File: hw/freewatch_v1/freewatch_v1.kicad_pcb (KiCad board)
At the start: 4 copper layers, 40 x 40 mm, 111 parts, among them P1 USB-MICRO-AB, P3 CONN_2, P6 CONN_2, P7 CONN_6, Q1 BSS138, Q2 BSS138, SW1 SW_PUSH, SW2 SW_PUSH, SW3 SW_PUSH, SW4 SW_PUSH, U1 PRTR5V0U2X, U10 MAX44009, U11 LSM303C, U12 MS5806-02BA, U13 ADP198, U14 LS013B7DH03, U15 EFM32GG330, U2 bq24072, U3 TPS780180300, U4 MAX17047, U5 TPS780180300, U6 M10478-A1, U7 MICRO_SDCARD_SPI, U8 ADP198, X1 32.768kHz, X2 48MHz

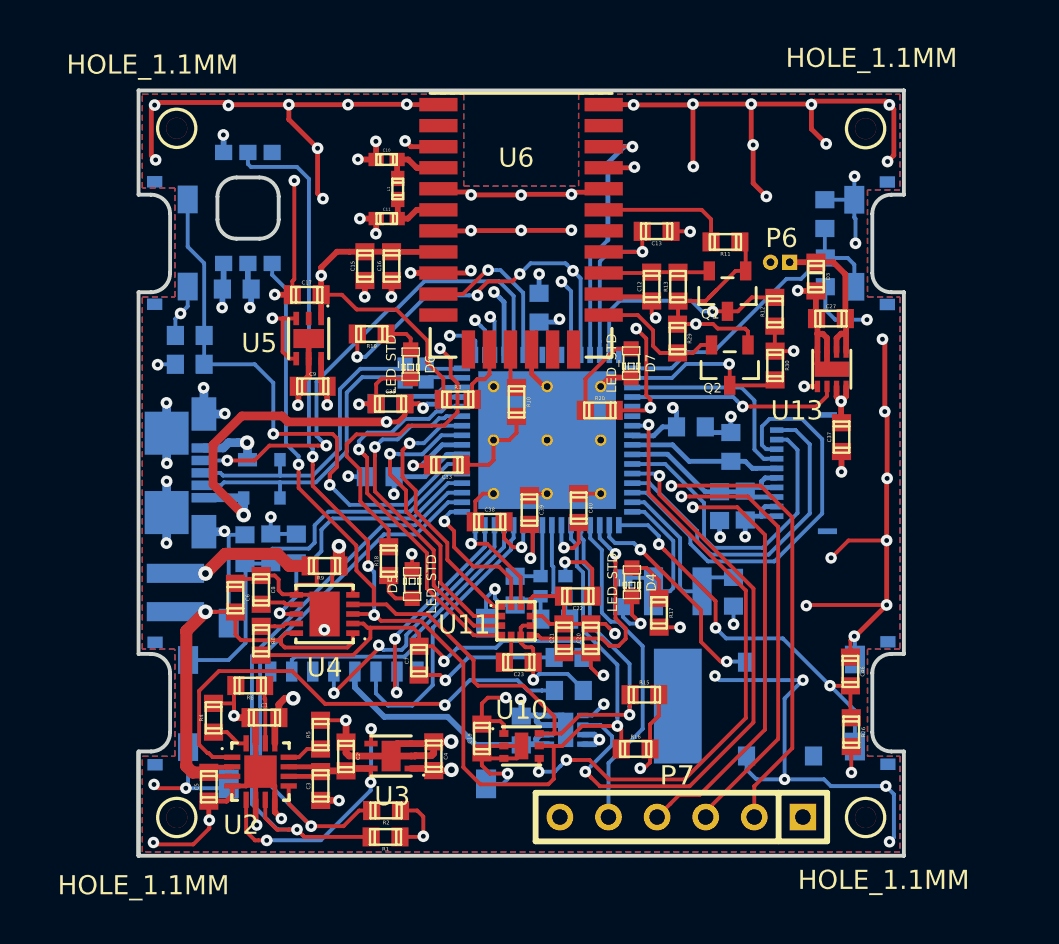
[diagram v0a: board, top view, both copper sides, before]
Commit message: hw: Add SPI flash memory for GPS module. Add SST25WF040B symbol and footprint.
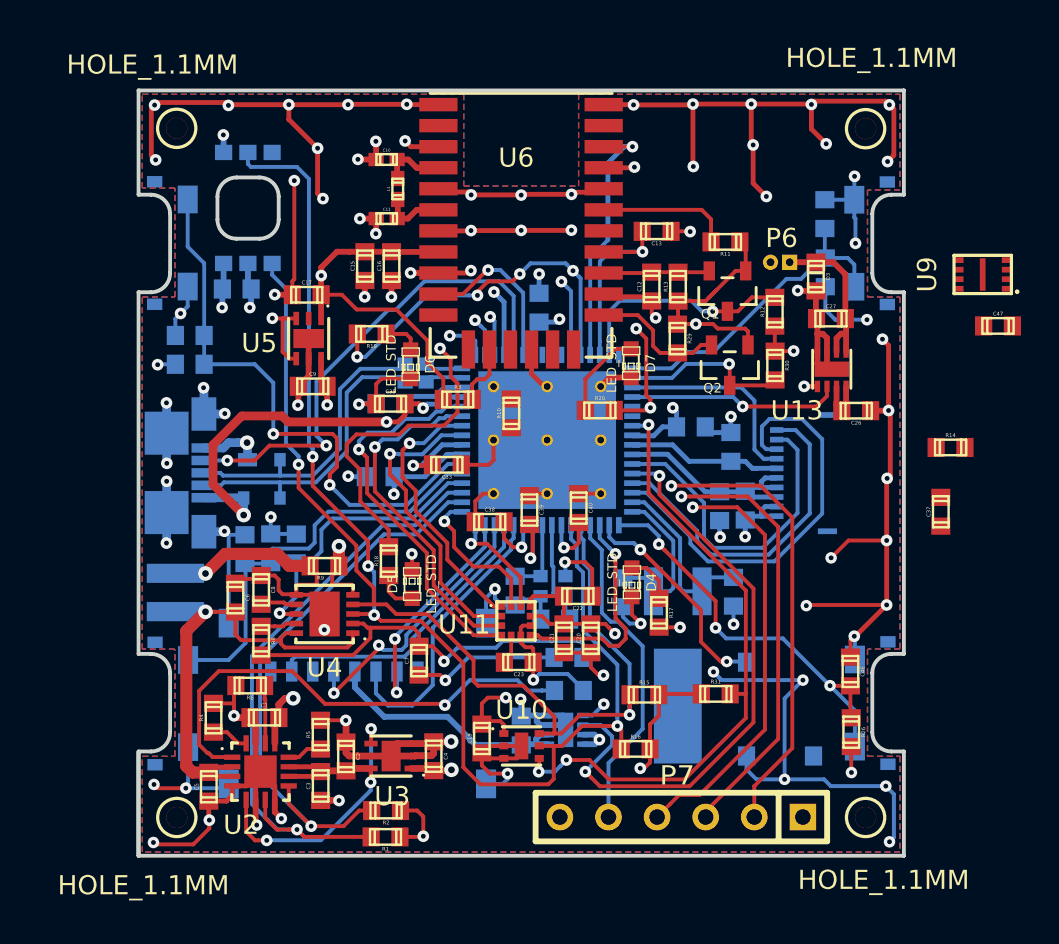
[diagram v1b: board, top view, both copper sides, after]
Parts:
- added C26: 10uF, Capacitors_SMD:c_0603, F.Cu at (123.8, 91.0)
- added C47: 100nF, Capacitors_SMD:c_0603, F.Cu at (131.2, 86.6)
- added R14: 10R, freewatch_footprints:r_0603, F.Cu at (128.7, 93.0)
- added R31: 100k, freewatch_footprints:r_0603, F.Cu at (116.5, 105.8)
- added U9: SST25WF040B, freewatch_footprints:USON_2X3, F.Cu at (130.4, 83.9)
- SW1, SW2, SW3, SW4: value SW_PUSH -> EVQ-P4MB3K
- moved C37 6.49 mm to (128.2, 96.3)
- moved R10 0.66 mm to (105.8, 91.2), turned to 90 degrees
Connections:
- C2 pad 1: Net-(C2-Pad1) -> +VIN
- C3 pad 1: Net-(C2-Pad1) -> +VIN
- C9 pad 1: VCC -> +VIN
- R10 pad 1: GND -> Net-(R10-Pad1)
- R10 pad 2: Net-(R10-Pad2) -> +1.8V
- U13 pad 7: VCC -> Net-(C26-Pad1)
- U13 pad 8: VCC -> Net-(C26-Pad1)
- U2 pad 10: Net-(C2-Pad1) -> +VIN
- U2 pad 11: Net-(C2-Pad1) -> +VIN
- U2 pad 5: Net-(C2-Pad1) -> +VIN
- U3 pad 4: Net-(C2-Pad1) -> +VIN
- U3 pad 6: Net-(C2-Pad1) -> +VIN
- U5 pad 4: VCC -> +VIN
- U5 pad 6: VCC -> +VIN
- U6 pad 14: Net-(R10-Pad2) -> Net-(R10-Pad1)
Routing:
- net +VIN: track 0.00 -> 23.5 mm, vias 0 -> 4
- net Net-(C2-Pad1): track 20.5 -> 0.00 mm, vias 3 -> 0
- net VCC: track 70.3 -> 66.8 mm, vias 23 -> 21
- net Net-(C26-Pad1): track 0.00 -> 2.74 mm
- net Net-(R10-Pad2): track 2.11 -> 0.00 mm
- net GND: track 294.7 -> 292.6 mm, vias 93 -> 92
- net LS_INT_N: track 31.9 -> 32.7 mm

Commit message: hw: Route SPI flash memory for GPS and 1.8V LDO + motor switch.
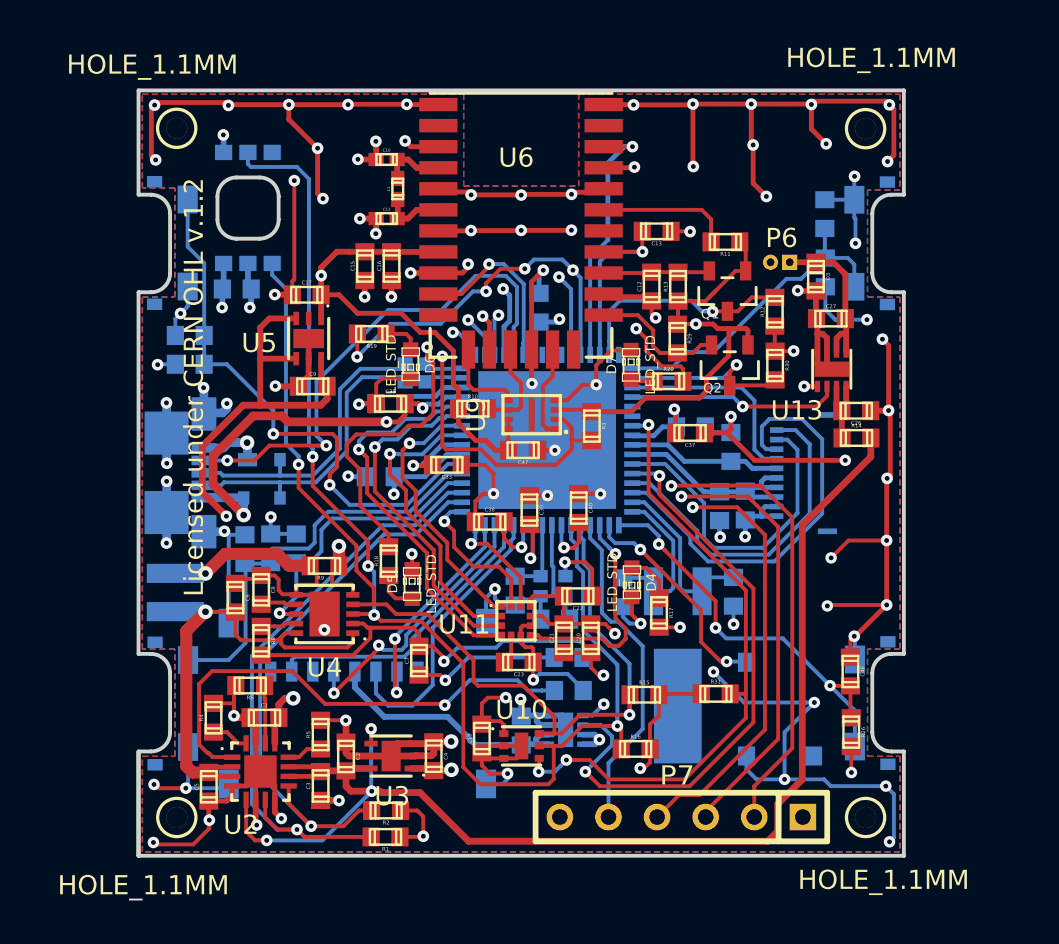
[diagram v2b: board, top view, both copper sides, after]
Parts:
- moved C47 25.7 mm to (106.4, 93.1), turned to 180 degrees
- moved U9 24.7 mm to (106.8, 91.2)
- moved C37 13.7 mm to (115.1, 92.2), turned to 180 degrees
- moved R3 7.15 mm to (110.0, 91.8), turned to 270 degrees
- moved R14 4.94 mm to (123.8, 92.5)
- moved R20 3.90 mm to (114.0, 89.5)
- moved R10 2.03 mm to (103.8, 90.9), turned to 0 degrees
- moved D7 0.09 mm to (112.0, 88.6), turned to 90 degrees
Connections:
- U5 pad 3: VCC -> +VIN
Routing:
- net +VIN: track 23.5 -> 108.9 mm
- net +1.8V: track 52.8 -> 72.1 mm
- net Net-(R3-Pad1): track 3.21 -> 21.6 mm, vias 0 -> 2
- net GND: track 292.6 -> 310.5 mm, vias 92 -> 99
- net Net-(R10-Pad1): track 0.00 -> 5.18 mm
- net Net-(U6-Pad16): track 0.00 -> 4.89 mm
- net Net-(U6-Pad12): track 0.00 -> 4.46 mm
- net Net-(D7-Pad1): track 4.68 -> 1.25 mm
- net VCC: track 66.8 -> 64.4 mm, vias 21 -> 20
- net /MCU_DISPLAY/LCD_BKL1: track 31.0 -> 28.8 mm, vias 6 -> 5
- net Net-(C26-Pad1): track 2.74 -> 4.17 mm
- net /MCU_DISPLAY/LCD_BKL2: track 54.3 -> 53.2 mm
- net /MCU_DISPLAY/SWDIO: track 45.0 -> 45.9 mm
- net /MCU_DISPLAY/SW_TL: track 29.9 -> 29.0 mm
- net USB_ID: track 26.2 -> 26.9 mm
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
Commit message: tom's little PCB cleanup
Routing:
- net VCC: track 64.4 -> 232.5 mm
- net GND: track 310.5 -> 329.0 mm, vias 99 -> 101
- net +VIN: track 108.9 -> 100.5 mm, vias 4 -> 7
- net /MCU_DISPLAY/SWDIO: track 45.9 -> 40.9 mm
- net /MCU_DISPLAY/SWCLK: track 46.9 -> 42.6 mm
- net BC_CHG_N: track 29.9 -> 27.7 mm
- net Net-(C6-Pad2): track 32.6 -> 30.4 mm
- net SD_EN: track 31.1 -> 29.0 mm
- net /MCU_DISPLAY/LCD_BKL2: track 53.2 -> 51.3 mm
- net SCL: track 65.3 -> 63.8 mm, vias 4 -> 5
- net AC_INT_MAG: track 11.9 -> 13.3 mm
- net /MCU_DISPLAY/SWDO: track 44.1 -> 42.7 mm
- net Net-(C32-Pad2): track 8.47 -> 7.22 mm
- net AC_CLK: track 14.2 -> 15.4 mm
- net /MCU_DISPLAY/SW_TL: track 29.0 -> 28.0 mm
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- added copper zone on Inner1.Cu, net +5V
- added copper zone on Inner1.Cu, net +VIN
- added copper zone on F.Cu, net Net-(C6-Pad2)
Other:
- outline, holes or cut-outs redrawn
- board text added: "Freewatch v1.0"
- board text added: "Program/SWD"

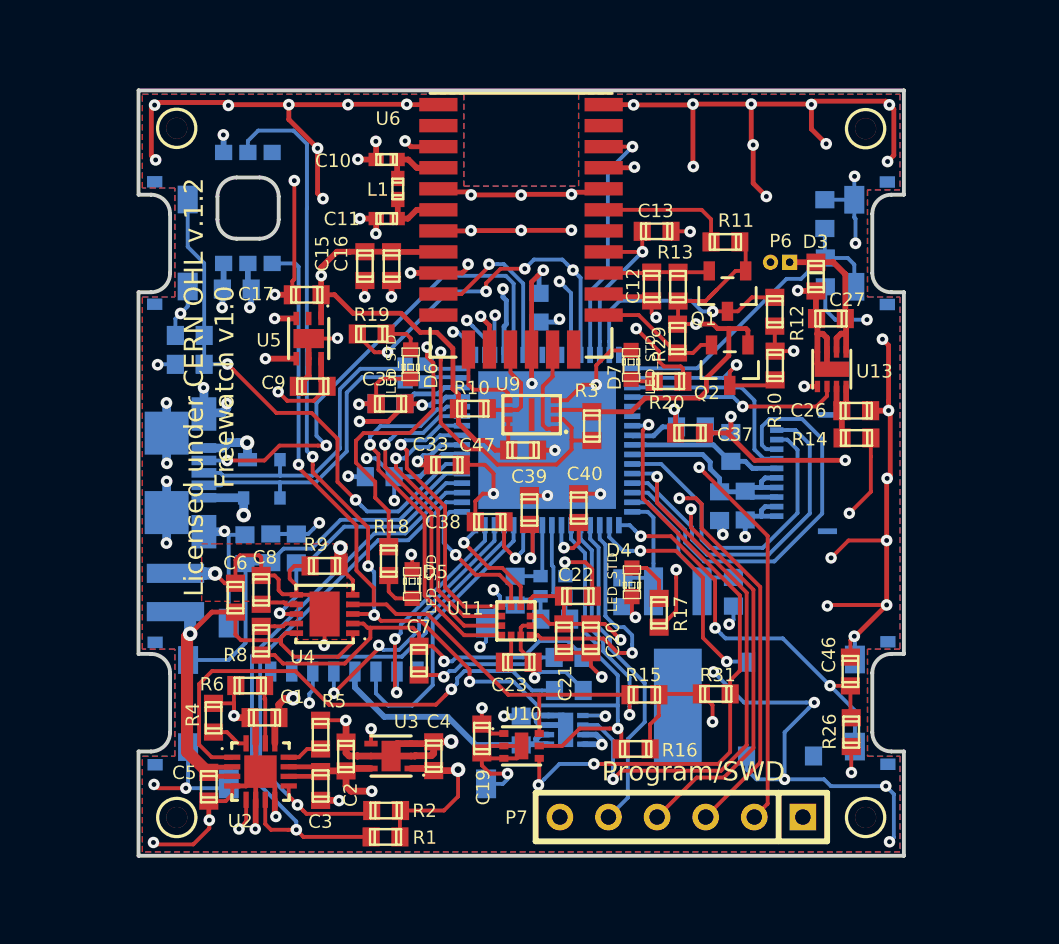
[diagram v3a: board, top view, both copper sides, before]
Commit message: hw: Final clean-up before prototype production
- Add more stitching vias
- Reduce copper planes clearance to 6 mils (was 10)
- Add copper pour keepouts to avoid antennas
- Undo copper plane on battery negative pin to fuel gauge (following datasheet layout recommendations).
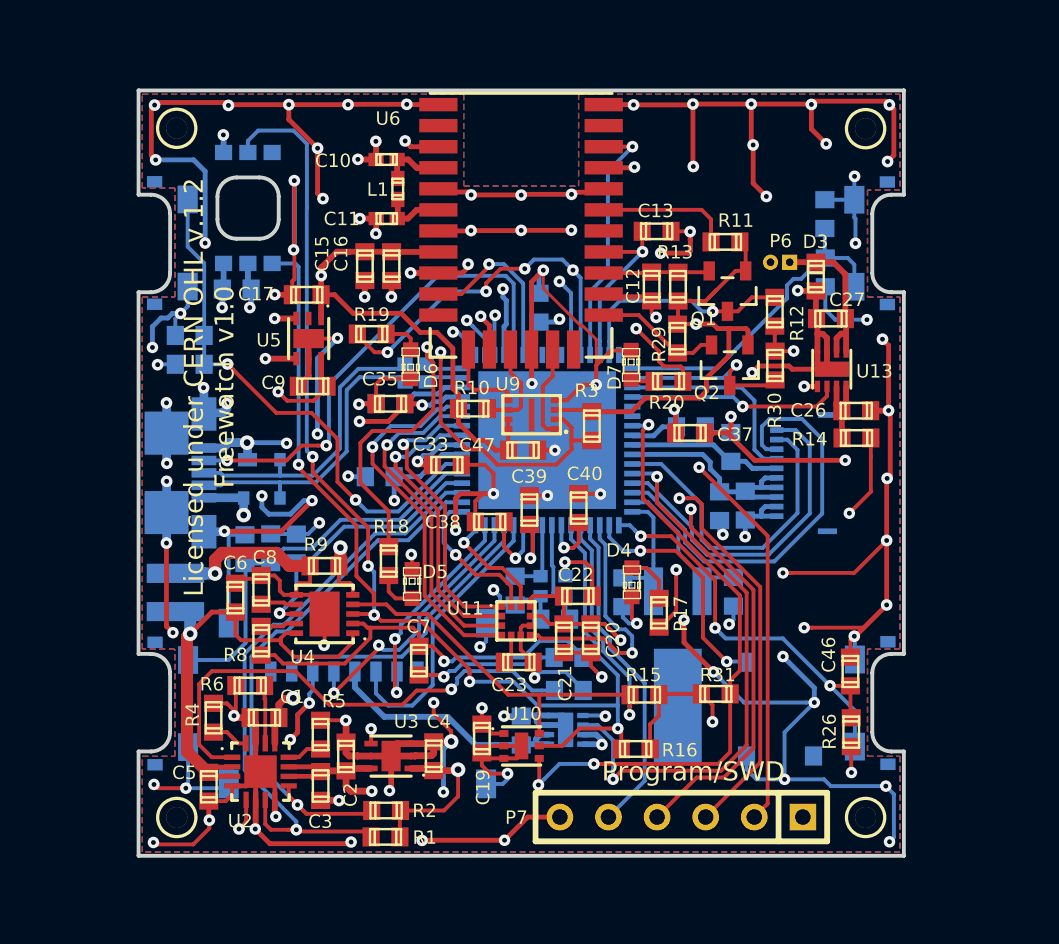
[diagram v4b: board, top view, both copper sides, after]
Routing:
- net GND: track 329.0 -> 417.2 mm, vias 101 -> 121
- net VCC: track 232.5 -> 228.6 mm, vias 20 -> 19
- net Net-(C6-Pad2): track 30.4 -> 32.7 mm
- net BC_CHG_N: track 27.7 -> 28.4 mm
- net BC_PGOOD_N: track 31.6 -> 32.2 mm
- removed copper zone on F.Cu, net Net-(C6-Pad2)

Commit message: hw: (Painfully) fix some via diameter errors.
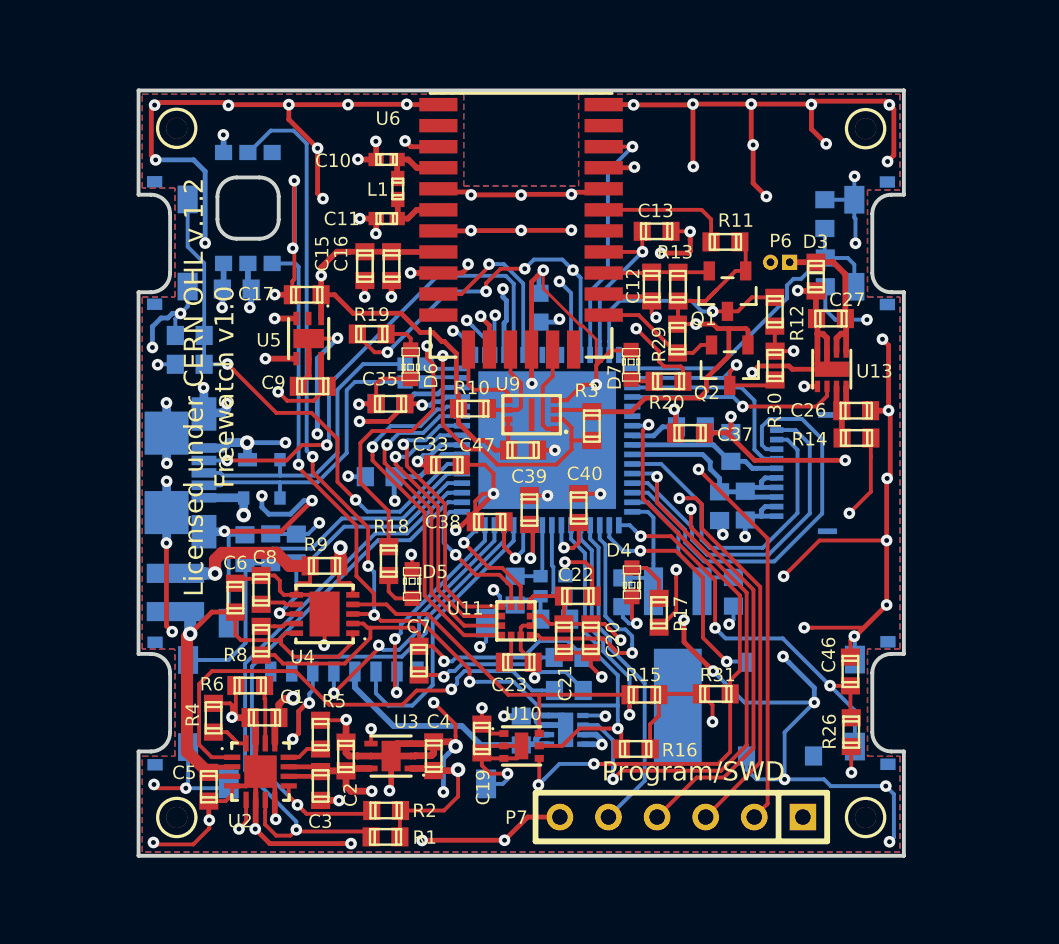
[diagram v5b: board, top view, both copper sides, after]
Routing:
- net +VIN: track 100.4 -> 99.8 mm
